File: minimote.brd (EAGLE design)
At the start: 85.6 x 54.2 mm, 41 parts, among them IC1 ATTINY441/841-SSU, J1 AVR_SPI_PROG_3X2PTH

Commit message: routed board
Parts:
- moved FRAME1 96.1 mm to (20.3, 57.1)
- moved U$11 58.3 mm to (25.4, 10.2), turned to 270 degrees
- moved U$12 55.9 mm to (25.4, 43.2), turned to 270 degrees
- moved U$6 39.4 mm to (73.7, 43.2), turned to 90 degrees
- moved D1 39.4 mm to (82.5, 20.3), turned to 180 degrees
- moved U$10 35.9 mm to (39.4, 27.9), turned to 270 degrees
- moved D3 32.0 mm to (82.5, 27.9), turned to 180 degrees
- moved U$7 31.8 mm to (61.0, 27.9), turned to 90 degrees
- moved U$5 29.6 mm to (73.7, 10.2), turned to 270 degrees
- moved U$8 27.5 mm to (50.8, 17.8), turned to 270 degrees
- moved D6 17.1 mm to (82.5, 35.6), turned to 180 degrees
- moved U$9 15.7 mm to (50.8, 38.1), turned to 270 degrees
- moved RN1 15.5 mm to (40.6, 48.3), turned to 0 degrees
- moved S1 11.5 mm to (39.4, 27.9)
- moved R8 11.4 mm to (22.9, 38.1)
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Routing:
- net GND: track 0.00 -> 166.7 mm, vias 0 -> 8
- net VCC: track 0.00 -> 158.5 mm, vias 0 -> 2
- net N$125: track 0.00 -> 114.9 mm, vias 0 -> 1
- net N$123: track 0.00 -> 110.5 mm, vias 0 -> 3
- net LED4: track 0.00 -> 104.9 mm, vias 0 -> 2
- net N$124: track 0.00 -> 85.3 mm, vias 0 -> 3
- net PAD0: track 0.00 -> 83.2 mm, vias 0 -> 2
- net V_USB: track 0.00 -> 63.4 mm, vias 0 -> 1
- net VBAT: track 0.00 -> 59.2 mm
- net RST: track 0.00 -> 53.8 mm, vias 0 -> 1
- net MISO: track 0.00 -> 53.3 mm, vias 0 -> 3
- net PAD6: track 0.00 -> 49.4 mm, vias 0 -> 1
- net PAD3: track 0.00 -> 47.6 mm, vias 0 -> 1
- net PAD1: track 0.00 -> 45.8 mm, vias 0 -> 1
- net N$7: track 0.00 -> 44.2 mm
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- added copper zone on layer 1, net GND
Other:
- outline, holes or cut-outs redrawn

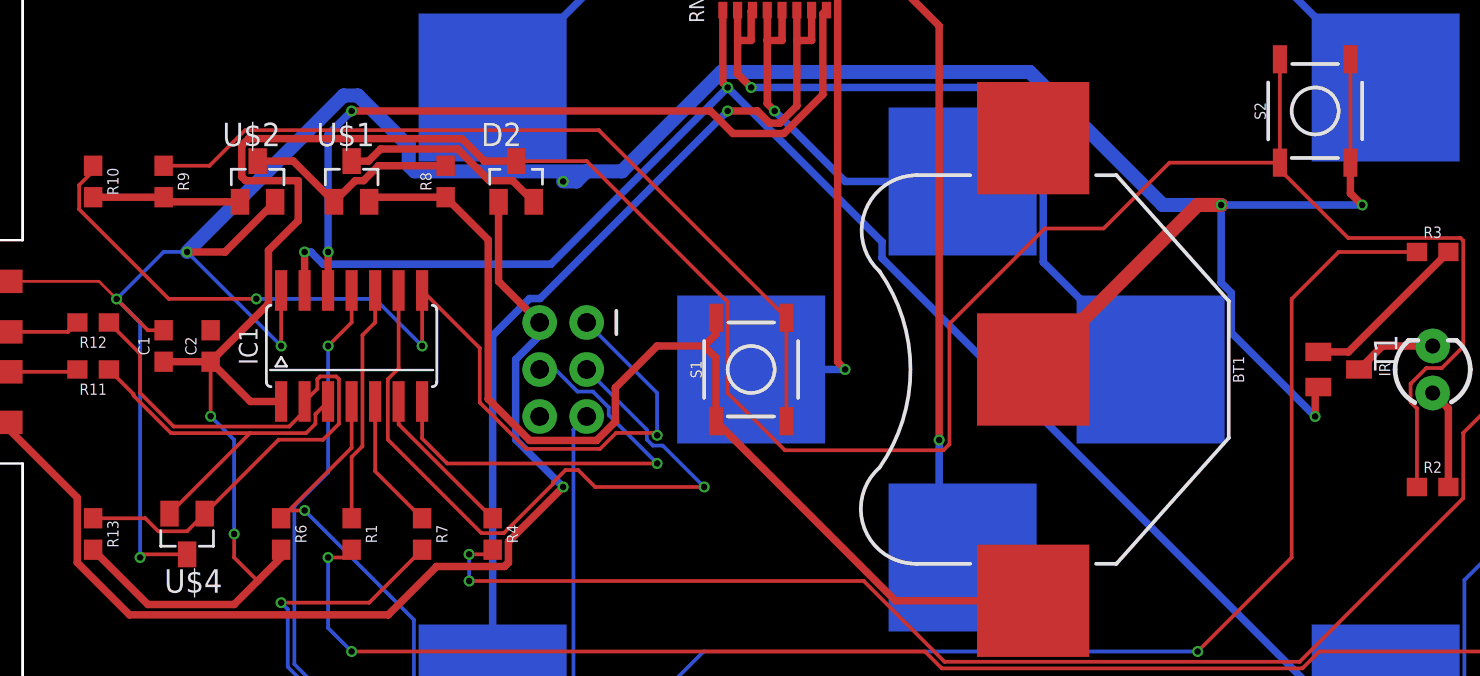
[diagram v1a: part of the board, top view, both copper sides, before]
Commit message: cleaned up ground traces
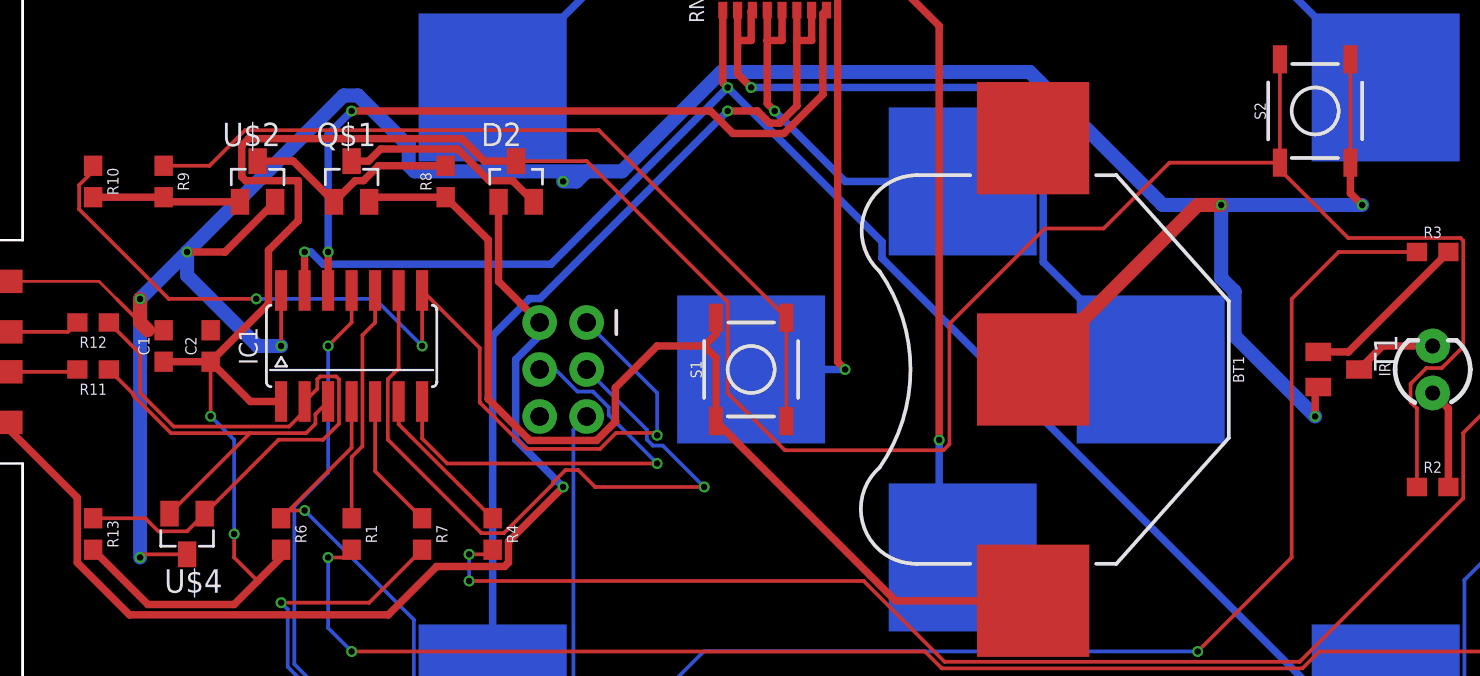
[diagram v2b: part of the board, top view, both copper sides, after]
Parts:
- renumbered U$1 to Q$1
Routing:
- net GND: track 166.7 -> 167.5 mm
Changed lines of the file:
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@@
 <attribute name="SF_SKU" value="COM-08720" x="69.85" y="41.91" size="1.778" layer="27" rot="R90" display="off"/>
 </element>
-<element name="U$1" library="minimote" package="SOT23" value="SI2301" x="17.78" y="38.1"/>
+<element name="Q$1" library="minimote" package="SOT23" value="SI2301" x="17.78" y="38.1"/>
 <element name="R8" library="SparkFun-Resistors" library_urn="urn:adsk.eagle:library:532" package="0603" package3d_urn="urn:adsk.eagle:package:39650/1" value="10k" x="22.86" y="38.1" rot="R90">
 <attribute name="PROD_ID" value="RES-07851" x="22.86" y="38.1" size="1.778" layer="27" rot="R90" display="off"/>
@@
 <wire x1="6.52" y1="17.95" x2="6.35" y2="17.78" width="0.2032" layer="1"/>
 <via x="6.35" y="17.78" extent="1-16" drill="0.35"/>
-<wire x1="6.35" y1="17.78" x2="6.35" y2="30.48" width="0.2032" layer="16"/>
-<wire x1="6.35" y1="30.48" x2="5.08" y2="31.75" width="0.2032" layer="16"/>
-<via x="5.08" y="31.75" extent="1-16" drill="0.35"/>
 <wire x1="5.08" y1="31.75" x2="6.77" y2="30.06" width="0.2032" layer="1"/>
 <wire x1="6.77" y1="30.06" x2="7.62" y2="30.06" width="0.2032" layer="1"/>
 <wire x1="13.97" y1="32.21" x2="13.97" y2="29.21" width="0.2032" layer="1"/>
 <via x="13.97" y="29.21" extent="1-16" drill="0.35"/>
-<wire x1="13.97" y1="29.21" x2="8.89" y2="34.29" width="0.2032" layer="16"/>
 <via x="8.89" y="34.29" extent="1-16" drill="0.35"/>
-<wire x1="8.89" y1="34.29" x2="7.62" y2="34.29" width="0.2032" layer="16"/>
-<wire x1="7.62" y1="34.29" x2="5.08" y2="31.75" width="0.2032" layer="16"/>
 <wire x1="54.61" y1="27.94" x2="63.5" y2="36.83" width="0.762" layer="1"/>
 <wire x1="63.5" y1="36.83" x2="64.77" y2="36.83" width="0.762" layer="1"/>
@@
 <wire x1="21.17905625" y1="38.6466" x2="20.8666" y2="38.95905625" width="0.762" layer="16"/>
 <wire x1="20.8666" y1="40.0934" x2="20.8666" y2="38.95905625" width="0.762" layer="16"/>
-<wire x1="64.77" y1="36.83" x2="61.61460625" y2="36.83" width="0.762" layer="16"/>
+<wire x1="64.77" y1="36.83" x2="63.5" y2="36.83" width="0.762" layer="16"/>
+<wire x1="63.5" y1="36.83" x2="61.61460625" y2="36.83" width="0.762" layer="16"/>
 <wire x1="37.7539625" y1="44.0154" x2="32.3851625" y2="38.6466" width="0.762" layer="16"/>
 <wire x1="32.3851625" y1="38.6466" x2="30.48" y2="38.6466" width="0.762" layer="16"/>
@@
 <wire x1="69.85" y1="26.82" x2="69.85" y2="25.4" width="0.4064" layer="1"/>
 <via x="69.85" y="25.4" extent="1-16" drill="0.35"/>
-<wire x1="69.85" y1="25.4" x2="65.3156" y2="29.9344" width="0.4064" layer="16"/>
-<wire x1="65.3156" y1="29.9344" x2="65.3156" y2="32.08729375" width="0.4064" layer="16"/>
-<wire x1="64.77" y1="32.63289375" x2="64.77" y2="36.83" width="0.4064" layer="16"/>
-<wire x1="65.3156" y1="32.08729375" x2="64.77" y2="32.63289375" width="0.4064" layer="16"/>
 <via x="72.39" y="36.83" extent="1-16" drill="0.35"/>
 <wire x1="71.755" y1="38.735" x2="71.755" y2="39.116" width="0.4064" layer="1"/>
@@
 <wire x1="71.755" y1="39.116" x2="71.755" y2="37.465" width="0.4064" layer="1"/>
 <wire x1="71.755" y1="37.465" x2="72.39" y2="36.83" width="0.4064" layer="1"/>
-<wire x1="64.77" y1="36.83" x2="72.39" y2="36.83" width="0.4064" layer="16"/>
+<wire x1="8.89" y1="34.29" x2="8.89" y2="33.02" width="0.762" layer="16"/>
+<wire x1="8.89" y1="33.02" x2="12.7" y2="29.21" width="0.762" layer="16"/>
+<wire x1="12.7" y1="29.21" x2="13.97" y2="29.21" width="0.762" layer="16"/>
+<wire x1="6.35" y1="31.75" x2="8.89" y2="34.29" width="0.762" layer="16"/>
+<wire x1="6.77" y1="30.06" x2="6.35" y2="30.48" width="0.762" layer="1"/>
+<wire x1="6.35" y1="30.48" x2="6.35" y2="31.75" width="0.762" layer="1"/>
+<wire x1="6.35" y1="17.78" x2="6.35" y2="31.75" width="0.762" layer="16"/>
+<via x="6.35" y="31.75" extent="1-16" drill="0.35"/>
+<wire x1="65.4934" y1="32.16094375" x2="65.4934" y2="29.7566" width="0.762" layer="16"/>
+<wire x1="65.4934" y1="29.7566" x2="69.85" y2="25.4" width="0.762" layer="16"/>
+<wire x1="64.77" y1="36.83" x2="64.77" y2="32.88434375" width="0.762" layer="16"/>
+<wire x1="64.77" y1="32.88434375" x2="65.4934" y2="32.16094375" width="0.762" layer="16"/>
+<wire x1="72.39" y1="36.83" x2="64.77" y2="36.83" width="0.762" layer="16"/>
 </signal>
 <signal name="VCC">
@@
 <signal name="VBAT">
 <contactref element="BT1" pad="1"/>
-<contactref element="U$1" pad="2"/>
+<contactref element="Q$1" pad="2"/>
 <contactref element="R8" pad="1"/>
 <contactref element="S1" pad="1"/>
@@
 </signal>
 <signal name="N$4">
-<contactref element="U$1" pad="1"/>
+<contactref element="Q$1" pad="1"/>
 <contactref element="R8" pad="2"/>
 <contactref element="U$2" pad="3"/>
@@
 </signal>
 <signal name="N$5">
-<contactref element="U$1" pad="3"/>
+<contactref element="Q$1" pad="3"/>
 <contactref element="D2" pad="2"/>
 <wire x1="27.62" y1="37" x2="26.4756" y2="38.1444" width="0.4064" layer="1"/>

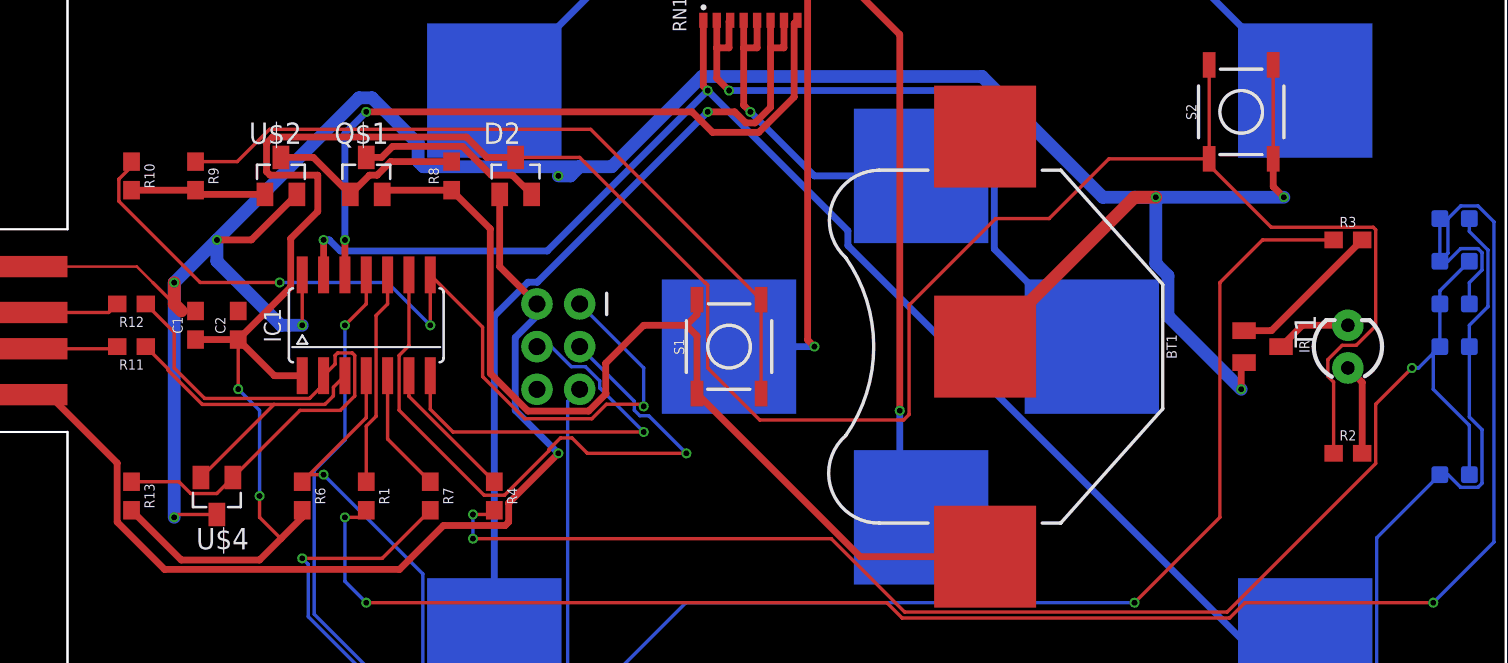
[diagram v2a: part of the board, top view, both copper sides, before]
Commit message: Cleaned up silkscreen
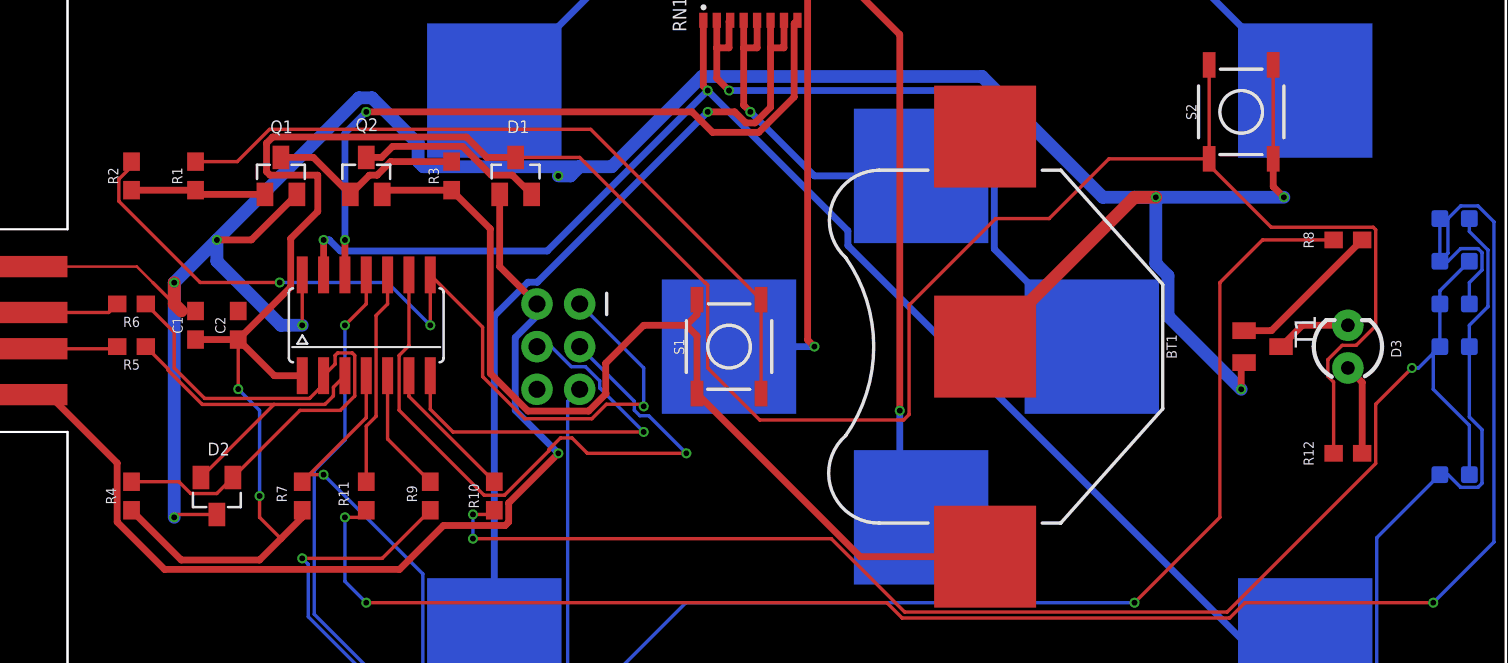
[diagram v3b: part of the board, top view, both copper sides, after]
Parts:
- removed IR: (no value), SparkFun-LED:LED_3MM
- removed R13: 1.5k, SparkFun-Resistors:0603
- removed U$4: AZ23C3V6, minimote:SOT23
- added D7, D8: BLUE, SparkFun-LED:LED-0603
- added R5: 100, SparkFun-Resistors:0603
- D1: value BLUE -> BAT54C; device SparkFun-LED:LED-0603 -> diode:SOT23
- D2: value BAT54C -> AZ23C3V6; device diode:SOT23 -> minimote:SOT23
- D3: value BLUE -> (none); device SparkFun-LED:LED-0603 -> SparkFun-LED:LED_3MM
- IC1: value ATTINY441/841-SSU -> ATTINY841
- R1: value 2k -> 22k
- R10: value 51k -> 2k
- R11: value 100 -> 2k
- R12: value 100 -> 22
- R2: value 22 -> 51k
- R3: value 330 -> 10k
- R4: value 2k -> 1.5k
- R6: value 4k7 -> 100
- R7: value 2k -> 4k7
- R8: value 10k -> 330
- R9: value 22k -> 2k
- moved R2 74.2 mm to (3.81, 38.1), turned to 270 degrees
- moved R12 72.9 mm to (76.2, 21.6), turned to 0 degrees
- moved D1 58.6 mm to (26.7, 38.1), flipped to the top, turned to 0 degrees
- moved R3 53.5 mm to (22.9, 38.1), turned to 90 degrees
- moved R8 53.5 mm to (76.2, 34.3), turned to 0 degrees
- moved R10 28.8 mm to (25.4, 19.1)
- moved D2 26.1 mm to (8.89, 19.1), turned to 180 degrees
- moved R9 23.6 mm to (21.6, 19.1)
- moved R1 21.6 mm to (7.62, 38.1)
- moved R4 21.6 mm to (3.81, 19.1)
- moved R11 16.6 mm to (17.8, 19.1), turned to 270 degrees
- moved R6 15.3 mm to (3.81, 30.5), turned to 180 degrees
- moved D4 10.2 mm to (82.5, 20.3)
- moved D6 7.62 mm to (82.5, 27.9)
- moved R7 7.62 mm to (14.0, 19.1)
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- renumbered Q$1 to Q2, U$10 to P6, U$11 to P7, U$12 to P8, U$13 to J2, U$2 to Q1, U$5 to P1, U$6 to P2, U$7 to P3, U$8 to P4, U$9 to P5
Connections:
- net D_M: now also D2.2, R5.1; no longer R11.1, U$4.2
- net D_P: now also D2.1, R4.1, R6.1; no longer R12.1, R13.1, U$4.1
- net GND: now also D2.3; no longer U$4.3
- net LED1: now also R9.1; no longer R7.1
- net LED2: now also R10.1; no longer R4.1
- net LED3: now also R11.1; no longer R1.1
- net LED4: now also R8.1; no longer R3.1
- net MISO: now also R2.1; no longer R10.1
- net N$1: now also D3.A, R12.2; no longer IR.A, R2.2
- net N$123: now also D7.C, D8.A, R11.2; no longer D4.C, D6.A, R1.2
- net N$124: now also D4.C, D6.A, D7.A, R10.2; no longer D1.C, D3.A, D4.A, R4.2
- net N$125: now also D4.A, D8.C, R9.2; no longer D1.A, D3.C, R7.2
- net N$2: now also D3.K; no longer IR.K
- net N$3: now also R8.2; no longer R3.2
- net N$4: now also R3.2; no longer R8.2
- net N$5: now also D1.2; no longer D2.2
- net N$6: now also R1.2, R2.2; no longer R10.2, R9.2
- net N$7: now also R1.1; no longer R9.1
- net N$8: now also R5.2; no longer R11.2
- net N$9: now also R6.2; no longer R12.2
- net RST: now also R7.1; no longer R6.1
- net VBAT: now also R3.1; no longer R8.1
- net VCC: now also D1.3, R12.1, R4.2, R7.2; no longer D2.3, R13.2, R2.1, R6.2
- net V_USB: now also D1.1; no longer D2.1
